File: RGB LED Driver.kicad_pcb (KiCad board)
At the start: 2 copper layers, 108 x 44.4 mm, 39 parts, among them J1 UART, J2 LED_STRIP_OUTPUT0, J3 5V_POWER_INPUT, J4 PWR_BTN, J5 LED_STRIP_OUTPUT1, J6 LED_STRIP_OUTPUT2, SW1 SW_Push, SW2 SW_Push, SW3 SW_Push, U1 ESP-12E, U2 AMS1117-3.3, U3 74LVC2G17, U4 74LVC2G17

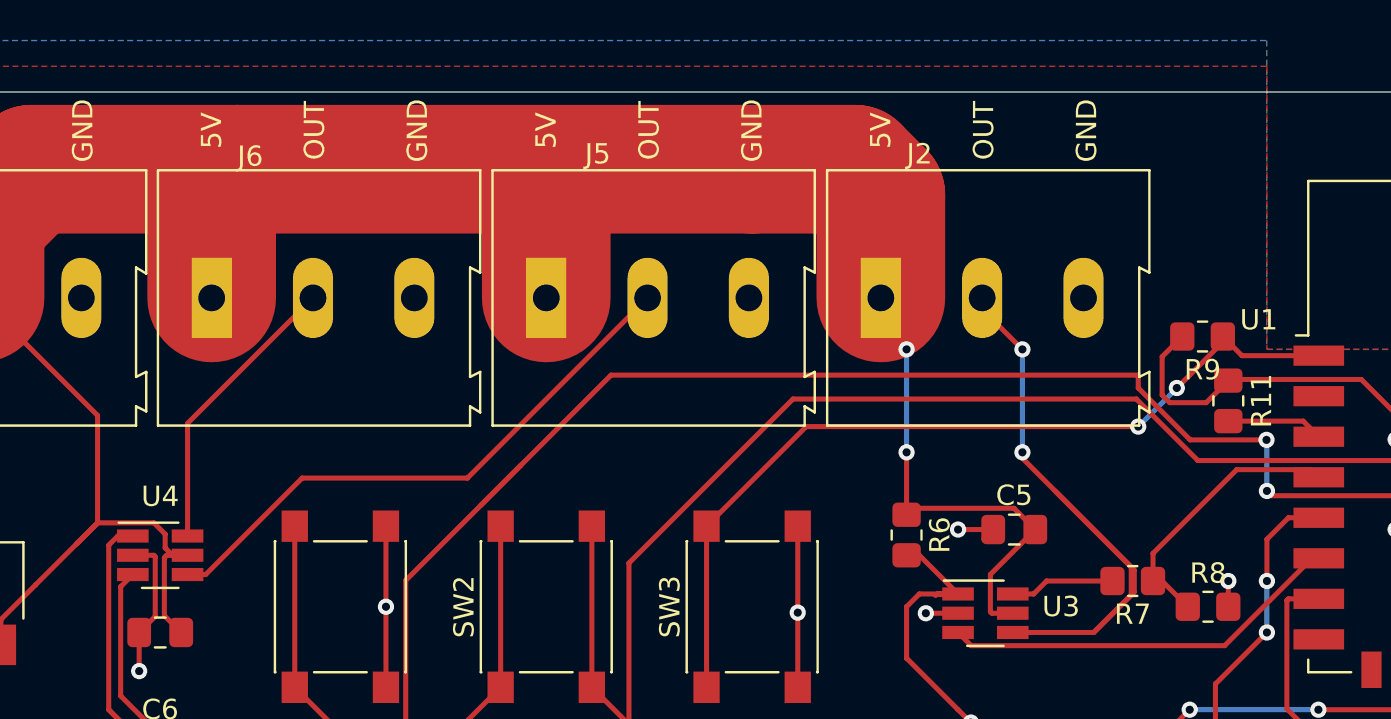
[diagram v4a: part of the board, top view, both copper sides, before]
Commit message: PCB updated and screw terminals moved
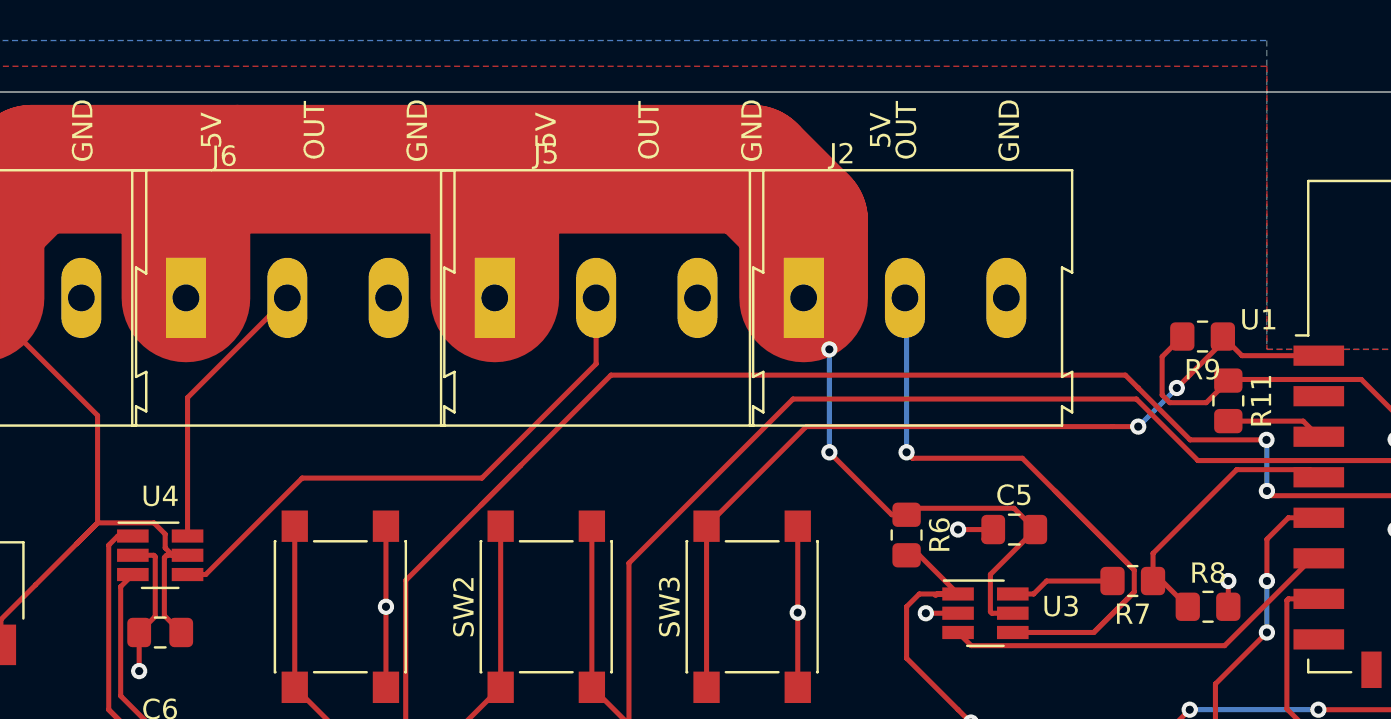
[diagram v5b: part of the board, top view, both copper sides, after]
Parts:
- moved J2 3.81 mm to (115.6, 53.3)
- moved J5 2.54 mm to (100.3, 53.3)
- moved J6 1.27 mm to (85.1, 53.3)
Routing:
- net +5V: track 149.9 -> 144.3 mm
- net Net-(J2-Pad2): track 34.0 -> 37.1 mm, vias 2 -> 1
- net Net-(J5-Pad2): track 28.4 -> 27.7 mm
- net Net-(J6-Pad2): track 14.3 -> 13.8 mm
